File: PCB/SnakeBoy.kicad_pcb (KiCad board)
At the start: 2 copper layers, 181.5 x 82.5 mm, 23 parts, among them SW1 X, SW2 A, SW3 Y, SW4 B, SW5 Start, SW6 Select, SW7 Power_SW, U1 ESP32-S3-DEVKITC-1-N16R8, U2 Joystick, U3 PAM8304 Module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

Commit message: Finished tracing the PCB
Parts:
- LS1: value Speaker -> Speaker_R
- LS2: value Speaker -> Speaker_L
- RV1: value R_Potentiometer_Dual -> Pot_Dual
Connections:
- A1 pad 1R: TFT_RST -> 3v3+
- A1 pad 2R: TFT_CS -> 3v7-
- A1 pad 3R: TFT_DC -> TFT_CS
- A1 pad 4R: TFT_DIN -> TFT_RST
- A1 pad 5R: TFT_CLK -> TFT_DC
- A1 pad 6R: 3v7+ -> TFT_DIN
- A1 pad 7R: TFT_BL -> TFT_CLK
- A1 pad 8R: 3v7- -> TFT_BL
- LS1 pad 1: unconnected-(LS1-Pad1) -> ROut-
- LS1 pad 2: unconnected-(LS1-Pad2) -> ROut+ vol
- LS2 pad 1: unconnected-(LS2-Pad1) -> LOut-
- LS2 pad 2: unconnected-(LS2-Pad2) -> LOut+ vol
- RV1 pad A1: unconnected-(RV1-PadA1) -> 3v7-
- RV1 pad A2: unconnected-(RV1-PadA2) -> LOut+
- RV1 pad A3: unconnected-(RV1-PadA3) -> LOut+ vol
- RV1 pad B1: unconnected-(RV1-PadB1) -> 3v7-
- RV1 pad B2: unconnected-(RV1-PadB2) -> ROut+
- RV1 pad B3: unconnected-(RV1-PadB3) -> ROut+ vol
- SW1 pad 2: 3v7+ -> 3v3+
- SW2 pad 2: 3v7+ -> 3v3+
- SW3 pad 2: 3v7+ -> 3v3+
- SW4 pad 2: 3v7+ -> 3v3+
- SW5 pad 2: 3v7+ -> 3v3+
- SW6 pad 2: unconnected-(SW6-Pad2) -> 3v3+
- U1 pad J1_1: unconnected-(U1-3V3-PadJ1_1) -> 3v3+
- U1 pad J1_12: unconnected-(U1-GPIO8-PadJ1_12) -> SD_MOSI
- U1 pad J1_15: unconnected-(U1-GPIO9-PadJ1_15) -> Joy_Y
- U1 pad J1_16: unconnected-(U1-GPIO10-PadJ1_16) -> Joy_X
- U1 pad J1_17: unconnected-(U1-GPIO11-PadJ1_17) -> SD_CS
- U1 pad J1_21: unconnected-(U1-5V0-PadJ1_21) -> 3v7+
- U1 pad J1_4: unconnected-(U1-GPIO4-PadJ1_4) -> TFT_DC
- U1 pad J1_5: unconnected-(U1-GPIO5-PadJ1_5) -> TFT_DIN
- U1 pad J1_6: unconnected-(U1-GPIO6-PadJ1_6) -> TFT_CLK
- U1 pad J1_7: unconnected-(U1-GPIO7-PadJ1_7) -> TFT_BL
- U1 pad J3_1: unconnected-(U1-GND-PadJ3_1) -> 3v7-
- U1 pad J3_10: unconnected-(U1-GPIO38-PadJ3_10) -> BT_X
- U1 pad J3_15: unconnected-(U1-GPIO45-PadJ3_15) -> BT_Start
- U1 pad J3_16: unconnected-(U1-GPIO48-PadJ3_16) -> BT_Select
- U1 pad J3_17: unconnected-(U1-GPIO47-PadJ3_17) -> BT_joymid
- U1 pad J3_18: unconnected-(U1-GPIO21-PadJ3_18) -> BT_B
- U1 pad J3_2: unconnected-(U1-U0TXD/GPIO43-PadJ3_2) -> BT_Y
- U1 pad J3_3: unconnected-(U1-U0RXD/GPIO44-PadJ3_3) -> BT_A
- U1 pad J3_4: unconnected-(U1-GPIO1-PadJ3_4) -> R_in
- U1 pad J3_5: unconnected-(U1-GPIO2-PadJ3_5) -> L_in
- U1 pad J3_6: unconnected-(U1-MTMS/GPIO42-PadJ3_6) -> SD_MISO
- U1 pad J3_7: unconnected-(U1-MTDI/GPIO41-PadJ3_7) -> SD_CLK
- U1 pad J3_8: unconnected-(U1-MTDO/GPIO40-PadJ3_8) -> TFT_RST
- U1 pad J3_9: unconnected-(U1-MTCK/GPIO39-PadJ3_9) -> TFT_CS
- U2 pad B2A: 3v7+ -> 3v3+
- U2 pad H1: 3v7+ -> 3v3+
- U2 pad V1: 3v7+ -> 3v3+
- U3 pad 3: unconnected-(U3-R_in-Pad3) -> R_in
- U3 pad 5: unconnected-(U3-L_in-Pad5) -> L_in
- U3 pad 6: unconnected-(U3-ROut--Pad6) -> ROut-
- U3 pad 7: unconnected-(U3-ROut+-Pad7) -> ROut+
- U3 pad 8: unconnected-(U3-LOut+-Pad8) -> LOut+
- U3 pad 9: unconnected-(U3-LOut--Pad9) -> LOut-
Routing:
- net 3v3+: track 0.00 -> 332.0 mm
- net 3v7+: track 0.00 -> 167.9 mm
- net LOut+: track 0.00 -> 130.2 mm
- net Joy_X: track 0.00 -> 122.0 mm
- net BT_Y: track 0.00 -> 119.7 mm
- net ROut-: track 0.00 -> 116.0 mm
- net ROut+: track 0.00 -> 111.3 mm
- net BT_B: track 0.00 -> 110.6 mm
- net Joy_Y: track 0.00 -> 98.8 mm
- net BT_Select: track 0.00 -> 89.0 mm
- net BT_X: track 0.00 -> 85.7 mm
- net LOut+ vol: track 0.00 -> 84.8 mm
- net BT_A: track 0.00 -> 84.4 mm
- net BT_joymid: track 0.00 -> 74.2 mm
- net TFT_DC: track 0.00 -> 54.4 mm
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- added copper zone on B.Cu, net 3v7-
- added copper zone on F.Cu, net 3v7-

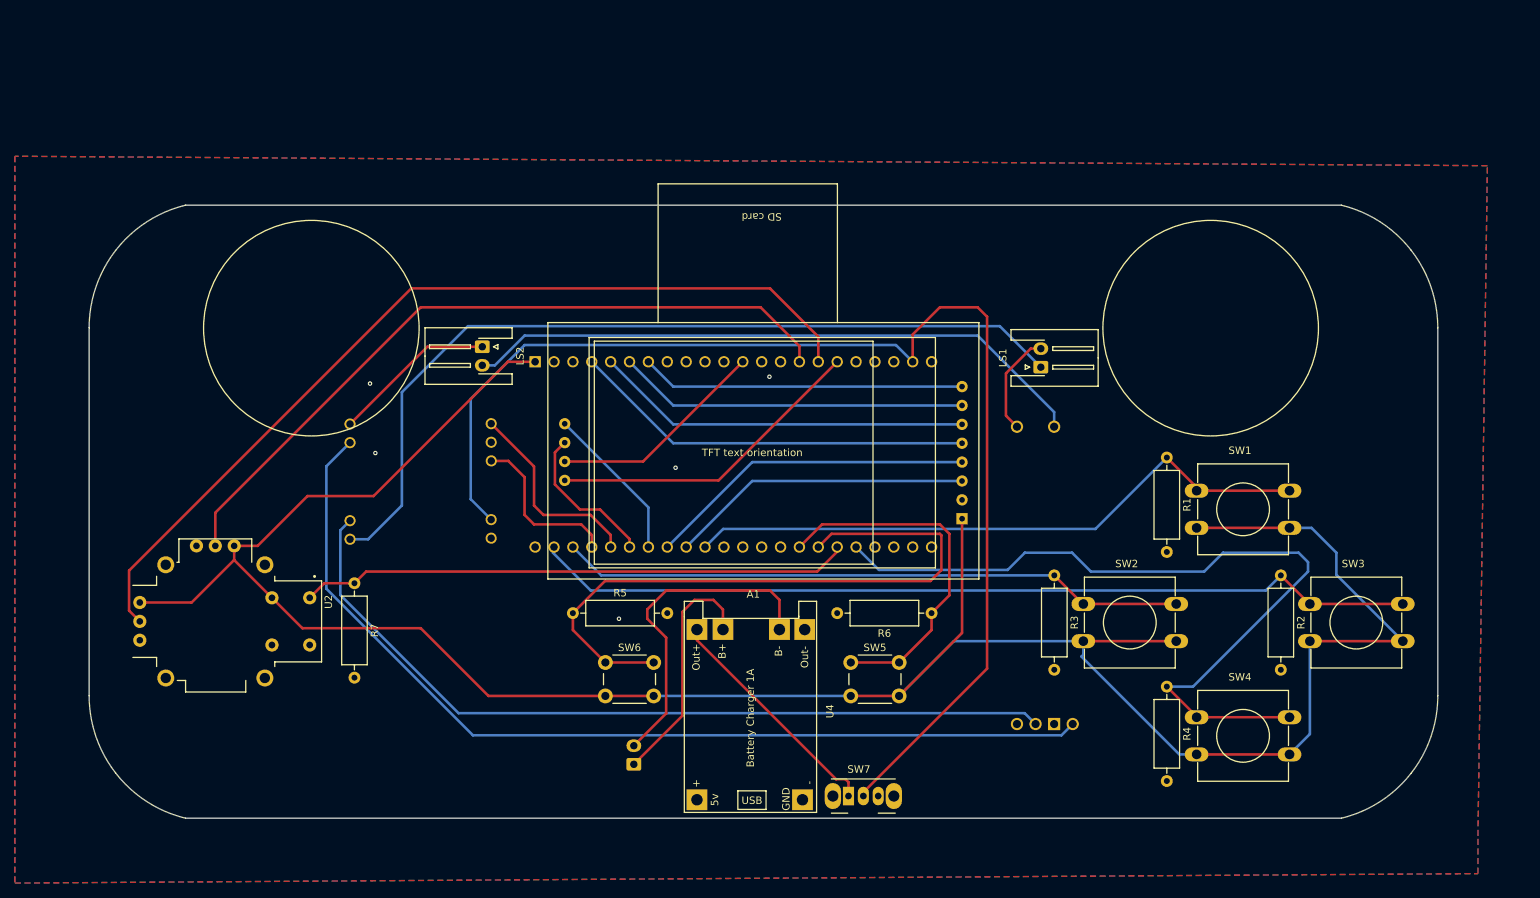
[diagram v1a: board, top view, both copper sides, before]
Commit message: Cloning the firmware source code from "@retroelec"
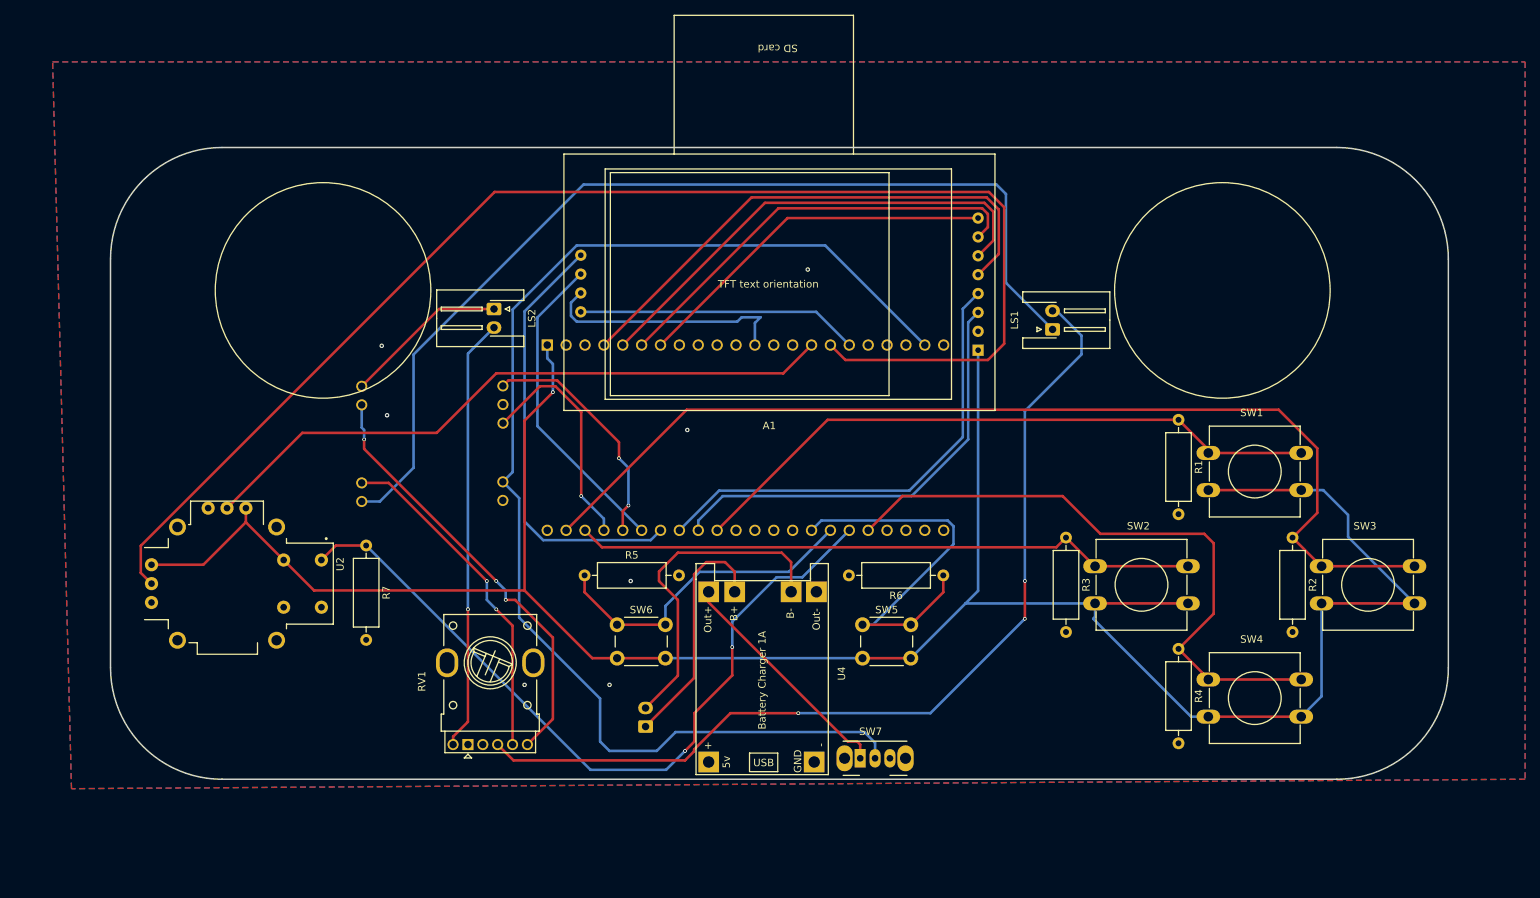
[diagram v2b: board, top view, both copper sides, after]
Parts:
- RV1: footprint slider:PS45M0MC2BR10KN -> Potentiometer_THT:Potentiometer_Bourns_PTV112-4_Dual_Vertical; moved to F.Cu
- moved RV1 80.9 mm to (110.5, 137.6)
- moved A1 22.8 mm to (150.9, 75.6)
- moved SW4 5.32 mm to (210.1, 128.8)
- moved SW7 5.32 mm to (163.3, 139.4)
- moved LS1 5.32 mm to (189.1, 81.7)
- moved R3 5.32 mm to (191.0, 109.7)
- moved SW2 5.32 mm to (194.9, 113.6)
- moved SW6 5.32 mm to (130.6, 121.5)
- moved LS2 5.32 mm to (114.0, 79.0)
- moved R5 5.32 mm to (126.2, 114.8)
- moved R7 5.32 mm to (96.8, 110.8)
- moved U2 5.32 mm to (78.1, 115.9)
- moved R1 5.32 mm to (206.1, 93.9)
- moved R2 5.32 mm to (221.4, 109.7)
- moved R4 5.32 mm to (206.1, 124.7)
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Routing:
- net ROut+ vol: track 13.9 -> 126.4 mm, vias 0 -> 3
- net LOut+: track 130.2 -> 58.5 mm, vias 0 -> 3
- net ROut+: track 111.3 -> 45.7 mm, vias 0 -> 2
- net Joy_X: track 122.0 -> 185.9 mm
- net BT_Select: track 89.0 -> 43.9 mm
- net SD_CLK: track 21.3 -> 58.8 mm
- net BT_joymid: track 74.2 -> 104.2 mm, vias 0 -> 2
- net LOut+ vol: track 84.8 -> 58.4 mm, vias 0 -> 1
- net BT_B: track 110.6 -> 85.5 mm
- net SD_MISO: track 20.3 -> 42.7 mm
- net BT_Y: track 119.7 -> 141.3 mm
- net TFT_RST: track 44.4 -> 63.5 mm
- net TFT_CS: track 40.8 -> 59.8 mm
- net ROut-: track 116.0 -> 134.6 mm
- net TFT_DC: track 54.4 -> 72.0 mm
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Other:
- board size 181.5 x 82.5 mm -> 180 x 85 mm

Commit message: Edited the PCB to match the firmware
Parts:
- removed RV1: Pot_Dual, Potentiometer_THT:Potentiometer_Bourns_PTV112-4_Dual_Vertical
- removed U3: PAM8304 Module, RAM:PAM8403
- added A2: max98357, Module-extra:max98357, F.Cu at (109.2, 119.4)
- moved R7 1.00 mm to (97.8, 110.8)
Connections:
- A1 pad 6R: TFT_DIN -> SD_MOSI
- A1 pad 7R: TFT_CLK -> SD_CLK
- LS1 pad 1: ROut- -> LOut-
- LS1 pad 2: ROut+ vol -> LOut+
- LS2 pad 2: LOut+ vol -> LOut+
- U1 pad J1_12: SD_MOSI -> unconnected-(U1-GPIO8-PadJ1_12)
- U1 pad J1_5: TFT_DIN -> SD_MOSI
- U1 pad J1_6: TFT_CLK -> SD_CLK
- U1 pad J3_4: R_in -> LRC
- U1 pad J3_5: L_in -> BCLK
- U1 pad J3_7: SD_CLK -> DIN
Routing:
- net LOut-: track 22.1 -> 181.9 mm, vias 0 -> 1
- net ROut-: track 134.6 -> 0.00 mm
- net ROut+ vol: track 126.4 -> 0.00 mm, vias 3 -> 0
- net LOut+: track 58.5 -> 182.6 mm, vias 3 -> 1
- net TFT_DIN: track 65.1 -> 0.00 mm
- net LOut+ vol: track 58.4 -> 0.00 mm, vias 1 -> 0
- net TFT_CLK: track 58.2 -> 0.00 mm
- net ROut+: track 45.7 -> 0.00 mm, vias 2 -> 0
- net SD_MOSI: track 33.8 -> 77.2 mm, vias 0 -> 1
- net L_in: track 32.1 -> 0.00 mm, vias 2 -> 0
- net R_in: track 31.2 -> 0.00 mm, vias 1 -> 0
- net DIN: track 0.00 -> 30.3 mm
- net BCLK: track 0.00 -> 21.3 mm
- net SD_CLK: track 58.8 -> 76.4 mm, vias 0 -> 1
- net 3v7+: track 169.9 -> 184.7 mm, vias 0 -> 4
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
